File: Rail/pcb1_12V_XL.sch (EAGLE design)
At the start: 116 parts, among them J1 638207222006, J10 638207222006, J11 638207222006, J12 638207222006, J2 638207222006, J4 61302211821, J8 61302211821, U1 ESP32-S3-DEVKITC-1-N8R2, U4 TLE9250VSJ, X2 B4P-VH

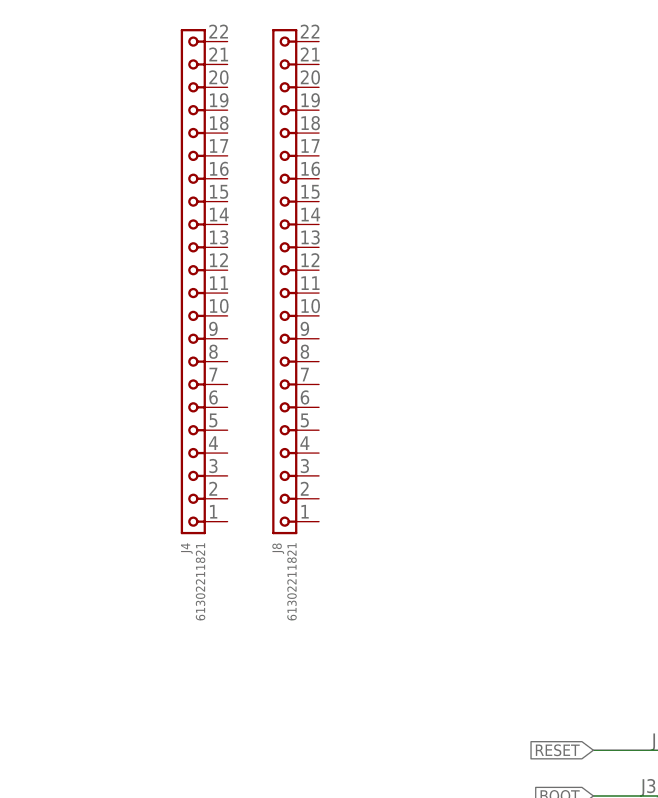
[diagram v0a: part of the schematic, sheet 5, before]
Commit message: change some Resistors
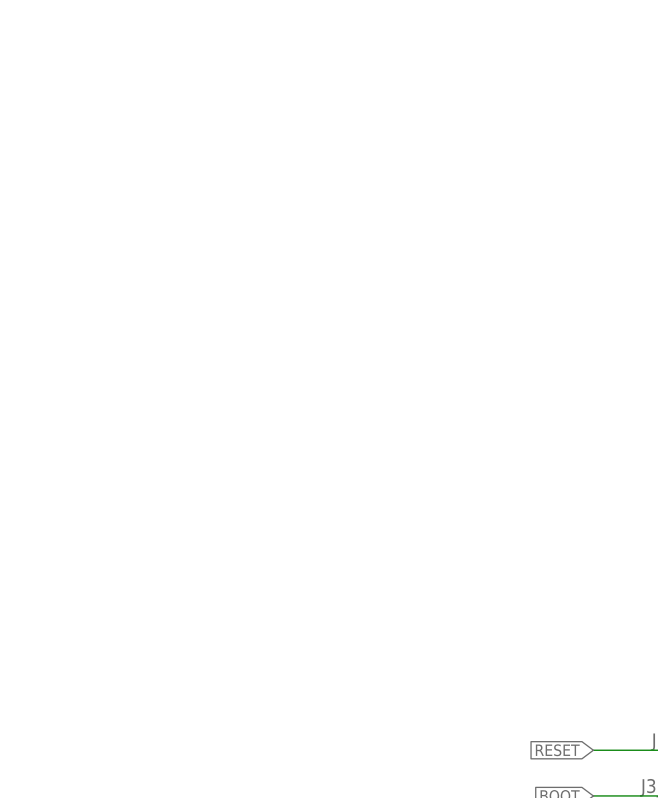
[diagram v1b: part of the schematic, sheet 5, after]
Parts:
- removed J4, J8: 61302211821, Wurth_Connectors_WR-PHD:6130XX11821_61302211821
- RX1, RX2, RX3, RX4, RX5, RX6, RX7, RX8: device Wurth_Resistor_WRIS-KWKB:WRIS-KWKB_0612_561020132023 -> resistor:R-EU_R1206
